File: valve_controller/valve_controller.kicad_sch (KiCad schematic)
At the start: 12 parts, among them J1 CDM1204-04A-FP-F9-67, U1 OPA197xD, U2 ADS1115IDGS, U3 MCP4728, U4 ESP32-S3

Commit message: First base
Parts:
- added C1, C2, C7, C8: 100nF, symbol Device:C
- added C3: 1uF, symbol Device:C
- added C4, C5: 22uF, symbol Device:C
- added C6: 10nF, symbol Device:C
- added D1, D2: LED, LED_SMD:LED_0805_2012Metric_Pad1.15x1.40mm_HandSolder, symbol RoverLibrary:LED
- added J2: T4141L12041-000, T4141L12041-000:TE_T4141L12041-000, symbol T4141L12041-000:T4141L12041-000
- added J3: CDM1204-04A-FP-F9-67, CDM1204-04A-FP-F9-67:CUI_CDM1204-04A-FP-F9-67, symbol CDM1204-04A-FP-F9-67:CDM1204-04A-FP-F9-67
- added JP1: SolderJumper_3_Open, symbol Jumper:SolderJumper_3_Open
- added P1: USB_C_Plug_USB2.0, symbol Connector:USB_C_Plug_USB2.0
- added R10, R11: 1k, symbol Device:R
- added R8: 10k, Resistor_SMD:R_0805_2012Metric_Pad1.20x1.40mm_HandSolder, symbol 0_RoverLibrary:R-10k
- added R9: R, symbol Device:R
- added SW1, SW2: SW_DPST_x2, symbol Switch:SW_DPST_x2
- added U5: TVS-SMDB03CE3, Package_SO:SOIC-8_3.9x4.9mm_P1.27mm, symbol RoverLibrary:TVS-SMDB03CE3/TR7TR-ND
- added U6: LDO-LM7805MPX/NOPB, Package_TO_SOT_SMD:TO-252-2, symbol RoverLibrary:LDO-TLE4284DV33ATMA1
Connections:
- net ALERT/RDY_ADC2 is gone; now on net ALERT/RDY_ADC1: U4.10 (GPIO5)
- net SCL_ADC2 is gone; now on net SCL_ADC1: U4.8 (GPIO3)
- net SDA_ADC2 is gone; now on net SDA_ADC1: U4.9 (GPIO4)
- net +24V: now also J2.1, JP1.1 (A), R11.1
- net +3.3V: now also U4.2 (VDD3P3), U4.20 (VDD3P3_RTC), U4.29 (VDD_SPI), U4.3 (VDD3P3), U4.46 (VDD3P3_CPU), U4.55 (VDDA), U4.56 (VDDA), C4.1, C5.1, R8.2
- net ALERT/RDY_ADC1: no longer U4.14 (GPIO9)
- net GND: now also C1.1, C2.1, C3.2, C4.2, C5.2, C6.2, C7.2, C8.2, D1.1 (K), D2.1 (K), J2.PE, P1.A1 (GND), P1.A12 (GND), P1.B1 (GND), P1.B12 (GND), R9.1, SW1.1 (A), SW2.1 (A), U5.5, U5.6, U5.7, U5.8, U6.1 (GND)
- net RDY_DAC1: now also U4.43 (GPIO38); no longer U4.18 (GPIO13)
- net SCL_ADC1: no longer U4.12 (GPIO7)
- net SCL_DAC1: now also U4.41 (GPIO36); no longer U4.16 (GPIO11)
- net SDA_ADC1: no longer U4.13 (GPIO8)
- net SDA_DAC1: now also U4.42 (GPIO37); no longer U4.17 (GPIO12)
- net USB_P: now reaches U4.26 (GPIO20/USB_D+)
- net USB_P: now also P1.A6 (D+), U5.3
- net EN: now reaches U4.4 (CHIP_PU)
- net EN: now also C2.2, C3.1, R8.1, SW2.2 (B)
- net BOOT: now reaches U4.5 (GPIO0)
- net BOOT: now also C1.2, SW1.2 (B)
- net RDY_DAC2 renamed USB_N
- net USB_N: now also P1.A7 (D-), U5.2
- net SCL_DAC2: no longer names the net of U4.23 (GPIO17)
- net SDA_DAC2: no longer names the net of U4.24 (GPIO18)
- new net: C6.1, C7.1, JP1.2 (C), U6.3 (INPUT)
- new net: D2.2 (A), R11.2
- new net: D1.2 (A), R10.2
- new net +3V3: C8.1, R10.1, U6.2 (OUTPUT)
- new net +5V: JP1.3 (B), P1.A4 (VBUS), P1.A9 (VBUS), P1.B4 (VBUS), P1.B9 (VBUS), U5.1
- new net CC: P1.A5 (CC), R9.2
- no-connect marks 0 -> 5
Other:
- note added: "Boot ESP32"
- note added: "Enable ESP32"
- note added: "Ethernet CONNECTOR"
- note added: "IO-Link CONNECTOR X8"
- note added: "LDO 3V3"
- note added: "POWER IN"
- note added: "Power LED"
- note added: "USB C"
- note removed: "CONNECTOR"
- moved on the sheet: J1, R1, R2, R3, R4, R5, R6, R7, U1, U2, U3, U4

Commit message: modif esp chip and power setup
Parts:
- removed JP1: SolderJumper_3_Open, symbol Jumper:SolderJumper_3_Open
- removed R5: 6.8K, symbol Device:R
- removed R6, R7: 20k, symbol Device:R
- removed R8: 10k, Resistor_SMD:R_0805_2012Metric_Pad1.20x1.40mm_HandSolder, symbol 0_RoverLibrary:R-10k
- removed U1: OPA197xD, Package_SO:SOIC-8_3.9x4.9mm_P1.27mm, symbol Amplifier_Operational:OPA197xD
- removed U4: ESP32-S3, Package_DFN_QFN:QFN-56-1EP_7x7mm_P0.4mm_EP4x4mm, symbol MCU_Espressif:ESP32-S3
- removed U5: TVS-SMDB03CE3, Package_SO:SOIC-8_3.9x4.9mm_P1.27mm, symbol RoverLibrary:TVS-SMDB03CE3/TR7TR-ND
- added C10: 470pF, symbol Device:C
- added C9: 1uF, symbol Device:C
- added D3, D4: LED, LED_SMD:LED_0805_2012Metric_Pad1.15x1.40mm_HandSolder, symbol RoverLibrary:LED
- added U1: LAN8720A, Package_DFN_QFN:VQFN-24-1EP_4x4mm_P0.5mm_EP2.5x2.5mm_ThermalVias, symbol Interface_Ethernet:LAN8720A
- added U4: CH340C, Package_SO:SOIC-16_3.9x9.9mm_P1.27mm, symbol Interface_USB:CH340C
- added U5: LM2596S-5, Package_TO_SOT_SMD:TO-263-5_TabPin3, symbol Regulator_Switching:LM2596S-5
- added U7: ESP32-WROOM-32, RF_Module:ESP32-WROOM-32, symbol RF_Module:ESP32-WROOM-32
- C3: value 1uF -> 22uF
- R4: value 13K -> 10k
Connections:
- net +24V: now also U5.1 (VIN)
- net +3V3: now also C3.1, C4.1, R1.1, R2.1, R3.1, R4.1, U2.8 (VDD), U3.1 (VDD), U1.1 (VDD2A), U1.19 (VDD1A), U1.9 (VDDIO), U7.2 (VDD)
- net +5V: now also C6.1, C7.1, U6.3 (INPUT), U5.2 (OUT), U5.4 (FB)
- net AIN0_ADC1: no longer R4.2
- net BOOT: now also C5.1, R4.2, U7.3 (EN)
- net EN: no longer C3.1
- net GND: now also C10.2, C9.2, D3.1 (K), D4.1 (K), U1.25 (VSS), U4.1 (GND), U5.3 (GND), U5.5 (~{ON}/OFF), U7.1 (GND), U7.15 (GND), U7.38 (GND), U7.39 (GND)
- net at J1.4: no longer R4.1
- net TX_P: now reaches J3.1
- net TX_P: now also U1.21 (TXP)
- net TX_N: now reaches J3.2
- net TX_N: now also U1.20 (TXN)
- net RX_P: now reaches J3.3
- net RX_P: now also U1.23 (RXP)
- net RX_N: now reaches J3.4
- net RX_N: now also U1.22 (RXN)
- removed net +3.3V: C4.1, C5.1, R1.1, R2.1, R3.1, U2.8 (VDD), U3.1 (VDD)
- new net: D3.2 (A), U1.2 (LED2/~{INTSEL})
- new net: D4.2 (A), U1.3 (LED1/REGOFF)
- new net: C10.1, C9.1, U1.6 (VDDCR)
- new net CRS_DV: U1.11 (CRS_DV/MODE2)
- new net MDC: U1.13 (MDC), U7.37 (IO23)
- new net MDIO: U1.12 (MDIO), U7.30 (IO18)
- new net RXD0: U1.8 (RXD0/MODE0), U7.34 (RXD0/IO3)
- new net RXD1: U1.7 (RXD1/MODE1), U7.26 (IO4)
- new net RXER: U1.10 (RXER/PHYAD0)
- new net TXD0: U1.17 (TXD0), U7.35 (TXD0/IO1)
- new net TXD1: U1.18 (TXD1), U7.24 (IO2)
- new net TXEN: U1.16 (TXEN)
- no-connect marks 5 -> 7
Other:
- note added: "5V Regulator"
- note added: "Ethernet transceiver"
- moved on the sheet: C6, C7, C8, J1, J3, R1, R2, R3, U2, U3, U6

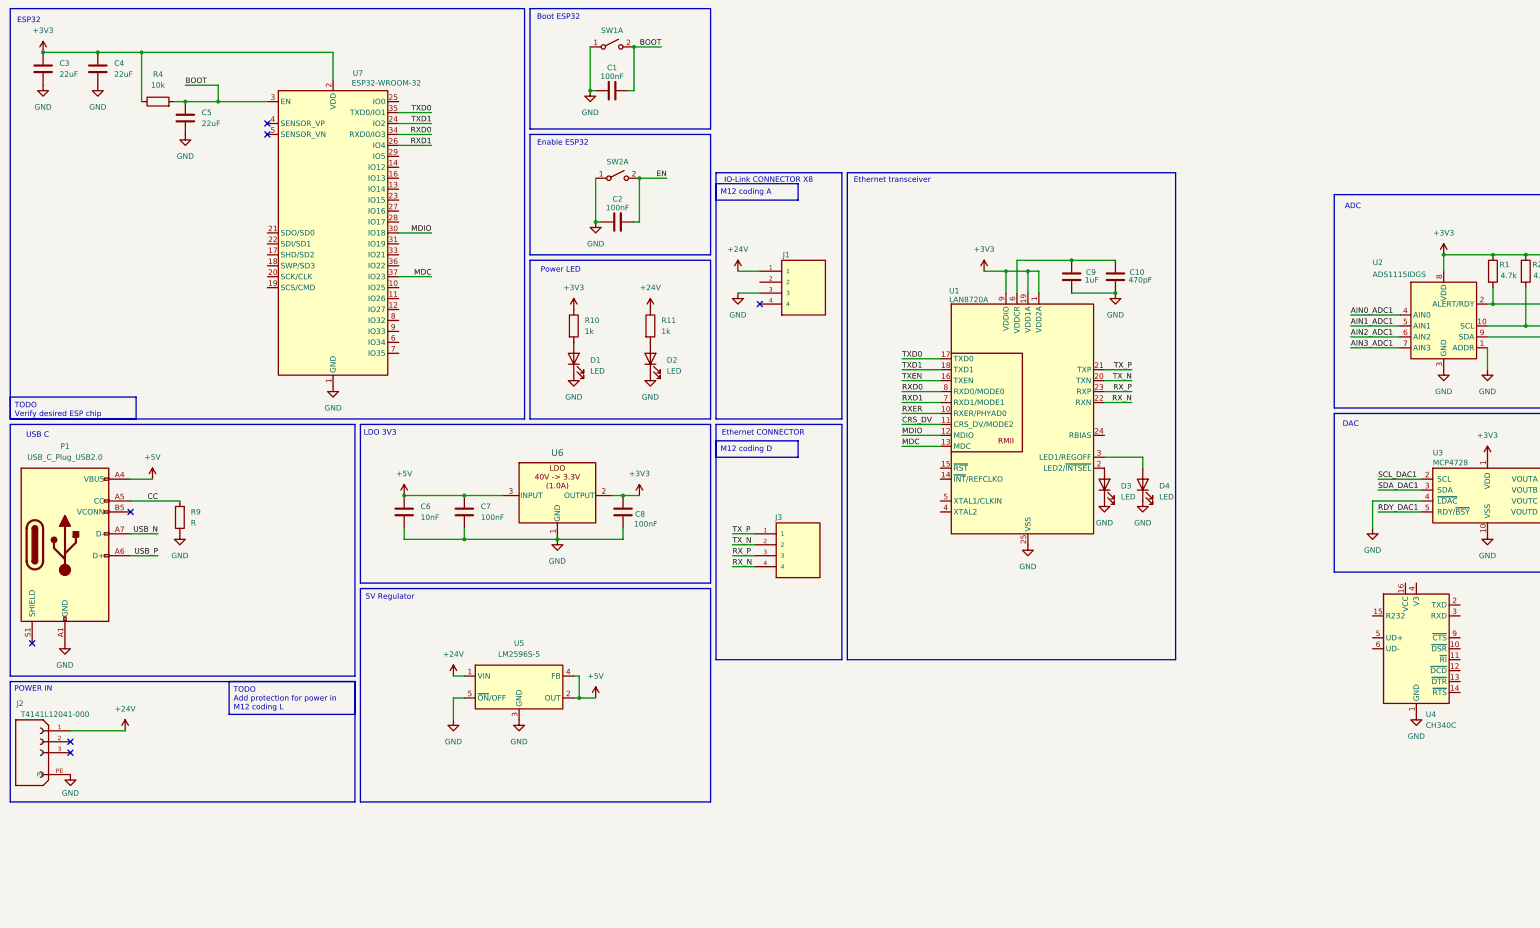
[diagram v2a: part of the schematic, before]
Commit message: Full ethernet interface
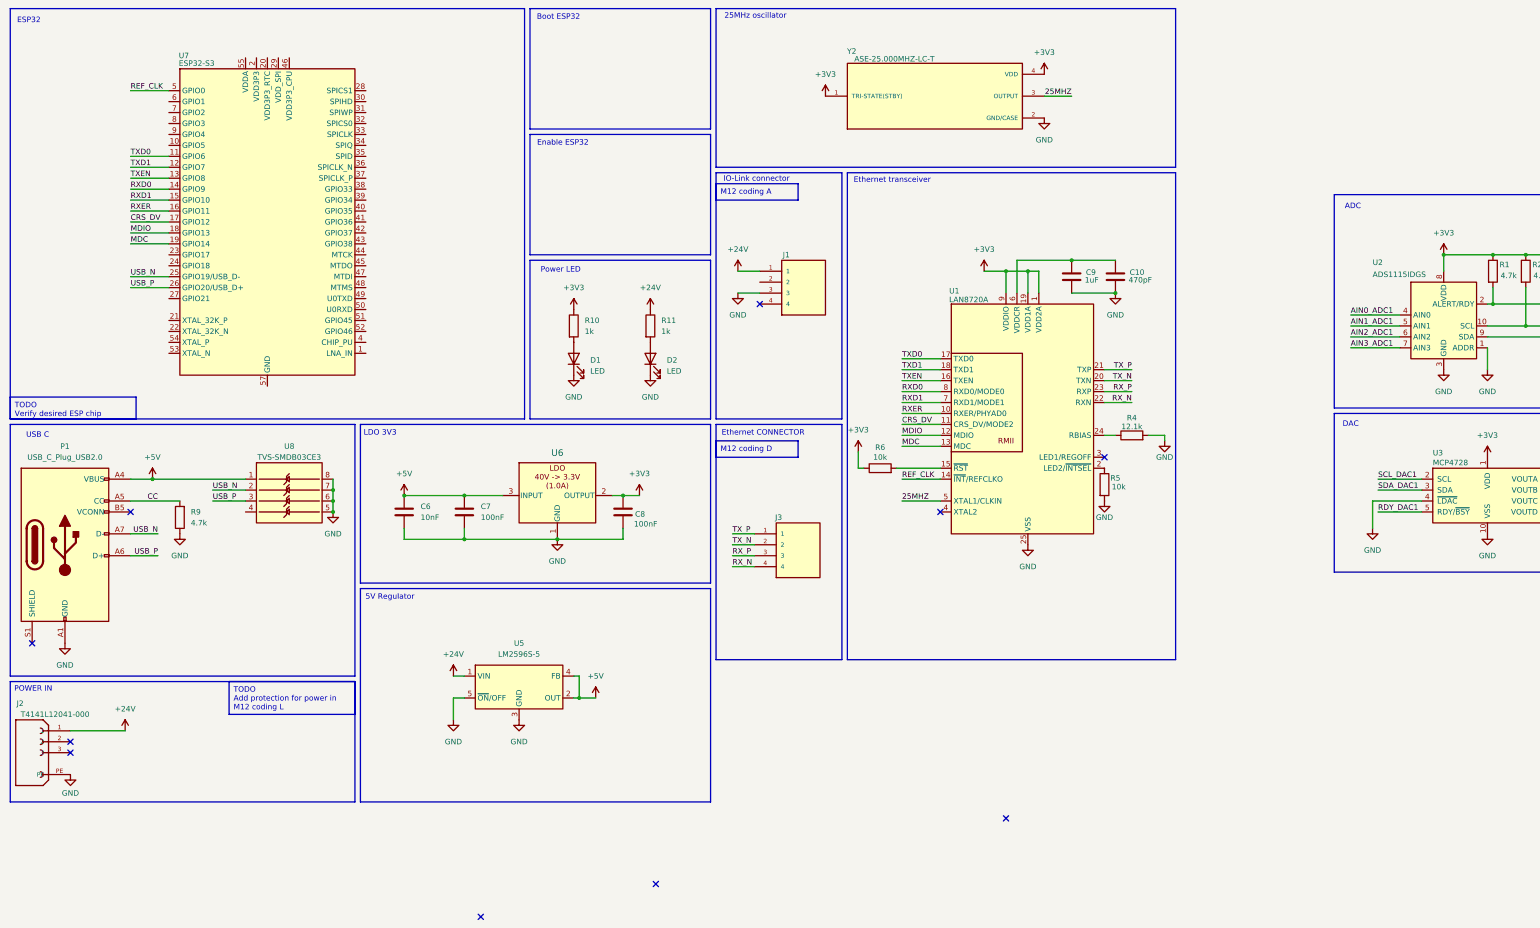
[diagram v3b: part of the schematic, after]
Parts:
- removed C1, C2: 100nF, symbol Device:C
- removed C3, C4, C5: 22uF, symbol Device:C
- removed D3, D4: LED, LED_SMD:LED_0805_2012Metric_Pad1.15x1.40mm_HandSolder, symbol RoverLibrary:LED
- removed SW1, SW2: SW_DPST_x2, symbol Switch:SW_DPST_x2
- removed U4: CH340C, Package_SO:SOIC-16_3.9x9.9mm_P1.27mm, symbol Interface_USB:CH340C
- removed U7: ESP32-WROOM-32, RF_Module:ESP32-WROOM-32, symbol RF_Module:ESP32-WROOM-32
- added R5, R6: 10k, symbol Device:R
- added U7: ESP32-S3, Package_DFN_QFN:QFN-56-1EP_7x7mm_P0.4mm_EP4x4mm, symbol MCU_Espressif:ESP32-S3
- added U8: TVS-SMDB03CE3, Package_SO:SOIC-8_3.9x4.9mm_P1.27mm, symbol 0_RoverLibrary:TVS-SMDB03CE3/TR7TR-ND
- added Y2: ASE-25.000MHZ-LC-T, ASE-25.000MHZ-LC-T:XTAL_ASE-25.000MHZ-LC-T, symbol ASE-25.000MHZ-LC-T:ASE-25.000MHZ-LC-T
- R10, R11: footprint (none) -> Resistor_SMD:R_0201_0603Metric
- R4: value 10k -> 12.1k
- R9: value R -> 4.7k
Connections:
- net BOOT is gone; now on net GND: R4.2
- net +3V3: now also R6.1, Y2.1 (TRI-STATE(STBY)), Y2.4 (VDD); no longer R4.1
- net +5V: now also U8.1
- net CRS_DV: now also U7.17 (GPIO12)
- net GND: now also R5.2, U8.5, U8.6, U8.7, U8.8, Y2.2 (GND/CASE)
- net MDC: now also U7.19 (GPIO14)
- net MDIO: now also U7.18 (GPIO13)
- net RXD0: now also U7.14 (GPIO9)
- net RXD1: now also U7.15 (GPIO10)
- net RXER: now also U7.16 (GPIO11)
- net TXD0: now also U7.11 (GPIO6)
- net TXD1: now also U7.12 (GPIO7)
- net TXEN: now also U7.13 (GPIO8)
- net USB_N: now also U7.25 (GPIO19/USB_D-), U8.2
- net USB_P: now also U7.26 (GPIO20/USB_D+), U8.3
- net REF_CLK: now reaches U1.14 (~{INT}/REFCLKO)
- net REF_CLK: now also U7.5 (GPIO0)
- net at U1.15 (~{RST}): now also R6.2
- net at U1.2 (LED2/~{INTSEL}): now also R5.1
- net at U1.24 (RBIAS): now also R4.1
- net 25MHZ: now reaches U1.5 (XTAL1/CLKIN)
- net 25MHZ: now also Y2.3 (OUTPUT)
- new net: U7.2 (VDD3P3), U7.3 (VDD3P3)
- new net: U7.55 (VDDA), U7.56 (VDDA)
- no-connect marks 7 -> 10
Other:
- note added: "25MHz oscillator"
- note added: "IO-Link connector"
- note removed: "IO-Link CONNECTOR X8"

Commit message: First layout  of pcb
Ready for review
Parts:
- removed R2, R3: 4.7k, symbol Device:R
- added C1, C2: 100nF, Capacitor_SMD:C_0805_2012Metric_Pad1.18x1.45mm_HandSolder, symbol 0_RoverLibrary:C-100nF
- added C3: 22uF, symbol Device:C
- added C4: 100nF, symbol Device:C
- added C5: 1uF, symbol Device:C
- added R7, R8: 4.7k, symbol Device:R
- added SW1, SW2: TS09-63-25-WT-160-SMT-TR, Button_Switch_SMD:SW_DIP_SPSTx01_Slide_6.7x4.1mm_W8.61mm_P2.54mm_LowProfile, symbol 0_RoverLibrary:PushButton-TS09-63-25-WT-160-SMT-TR
- R1: value 4.7k -> 10k
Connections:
- net SCL_ADC1 is gone; now on net SCL: U2.10 (SCL)
- net SCL_DAC1 is gone; now on net SCL: U3.2 (SCL)
- net SDA_ADC1 is gone; now on net SDA: U2.9 (SDA)
- net SDA_DAC1 is gone; now on net SDA: U3.3 (SDA)
- net +3V3: now also U7.2 (VDD3P3), U7.20 (VDD3P3_RTC), U7.3 (VDD3P3), U7.55 (VDDA), U7.56 (VDDA), C3.1, C4.1, R7.1, R8.1
- net GND: now also C1.1, C2.1, C3.2, C4.2, C5.2, SW1.1, SW2.1
- net SCL: now reaches U7.38 (GPIO33)
- net SCL: now also R7.2
- net SDA: now reaches U7.39 (GPIO34)
- net SDA: now also R8.2
- net CHIP_PU: now reaches U7.4 (CHIP_PU)
- net CHIP_PU: now also R1.2, C2.2, C5.1, SW2.2
- net ALERT/RDY_ADC1: no longer names the net of U2.2 (ALERT/RDY)
- net ALERT/RDY_ADC1: no longer R1.2
- net RDY_DAC1: no longer names the net of U3.5 (RDY/~{BSY})
- new net BOOT: C1.2, SW1.2
- no-connect marks 10 -> 22
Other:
- moved on the sheet: C10, C9, R4, R5, R6, U1, U2, U3, U7, Y2
